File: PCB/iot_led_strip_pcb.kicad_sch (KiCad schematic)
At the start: 39 parts, among them J1 I2C Expansion, J2 Conn_01x03_Socket, J3 GT-USB-7010ASV, J4 Barrel_Jack_Switch_Pin3Ring, J5 TC2050-IDC_Cortex-M, J6 Conn_01x03_Socket_Solderwire, J8 UART, Q1 BSS138, SW1 RESET, SW2 FLASH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

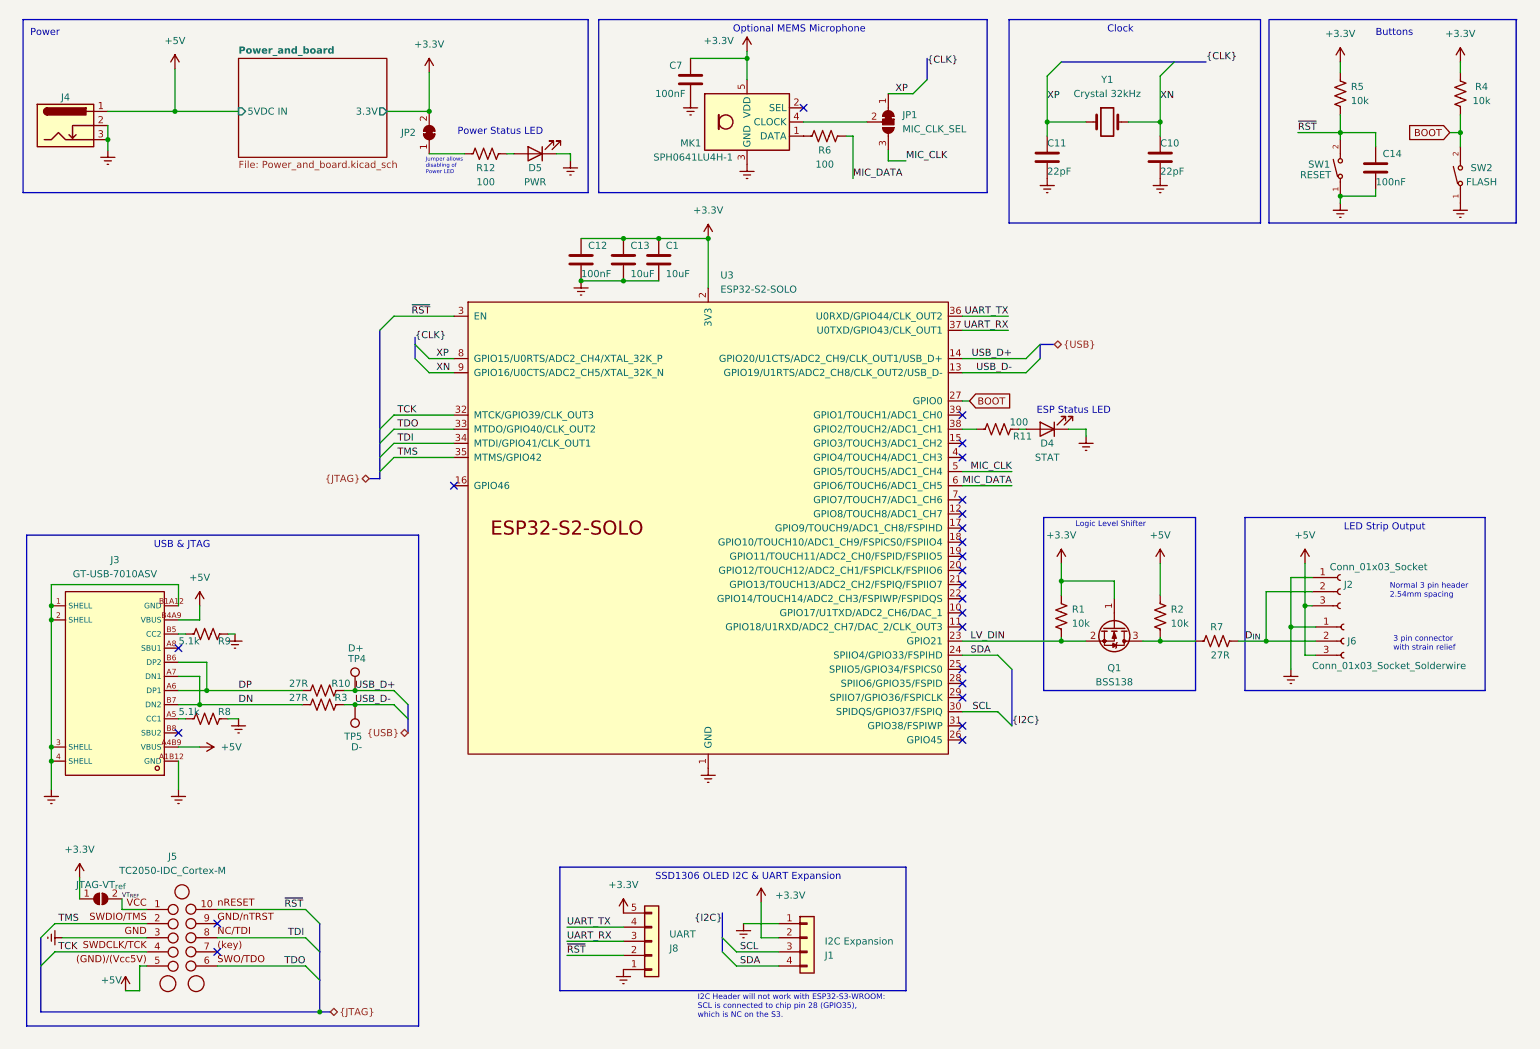
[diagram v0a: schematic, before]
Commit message: Major schematic update for v2.3
This was my first real PCB project, and looking back with a couple
months of hindsight I made some mistakes. Some best practices for
driving WS2812B strips weren't followed in my original version, and
I've updated the schematic to reflect what I've learned and what
improvements needed to be made.

* Warning added to README about current version
* Schematic reorganized into tiles
* RTC clock removed
* OLED and I2C headers removed
* JTAG footprint updated
* Pin header output replaced with screw terminal
* Hole size for power injection header increased
* Added whole system fuse and PTC fuse to protect ESP32
* Added reverse polarity protection and re-added ability to disconnect
  USB Vbus from Vdd, so it's possible to program when the strip is
  connected to 12V without frying your computer

There are a couple other improvements that could still be made to the
schematic (removing the solderwire connector for example) but it remains to
be seen if I'm going to go back and re-design the PCB to incorporate
these changes or move onto newer projects.
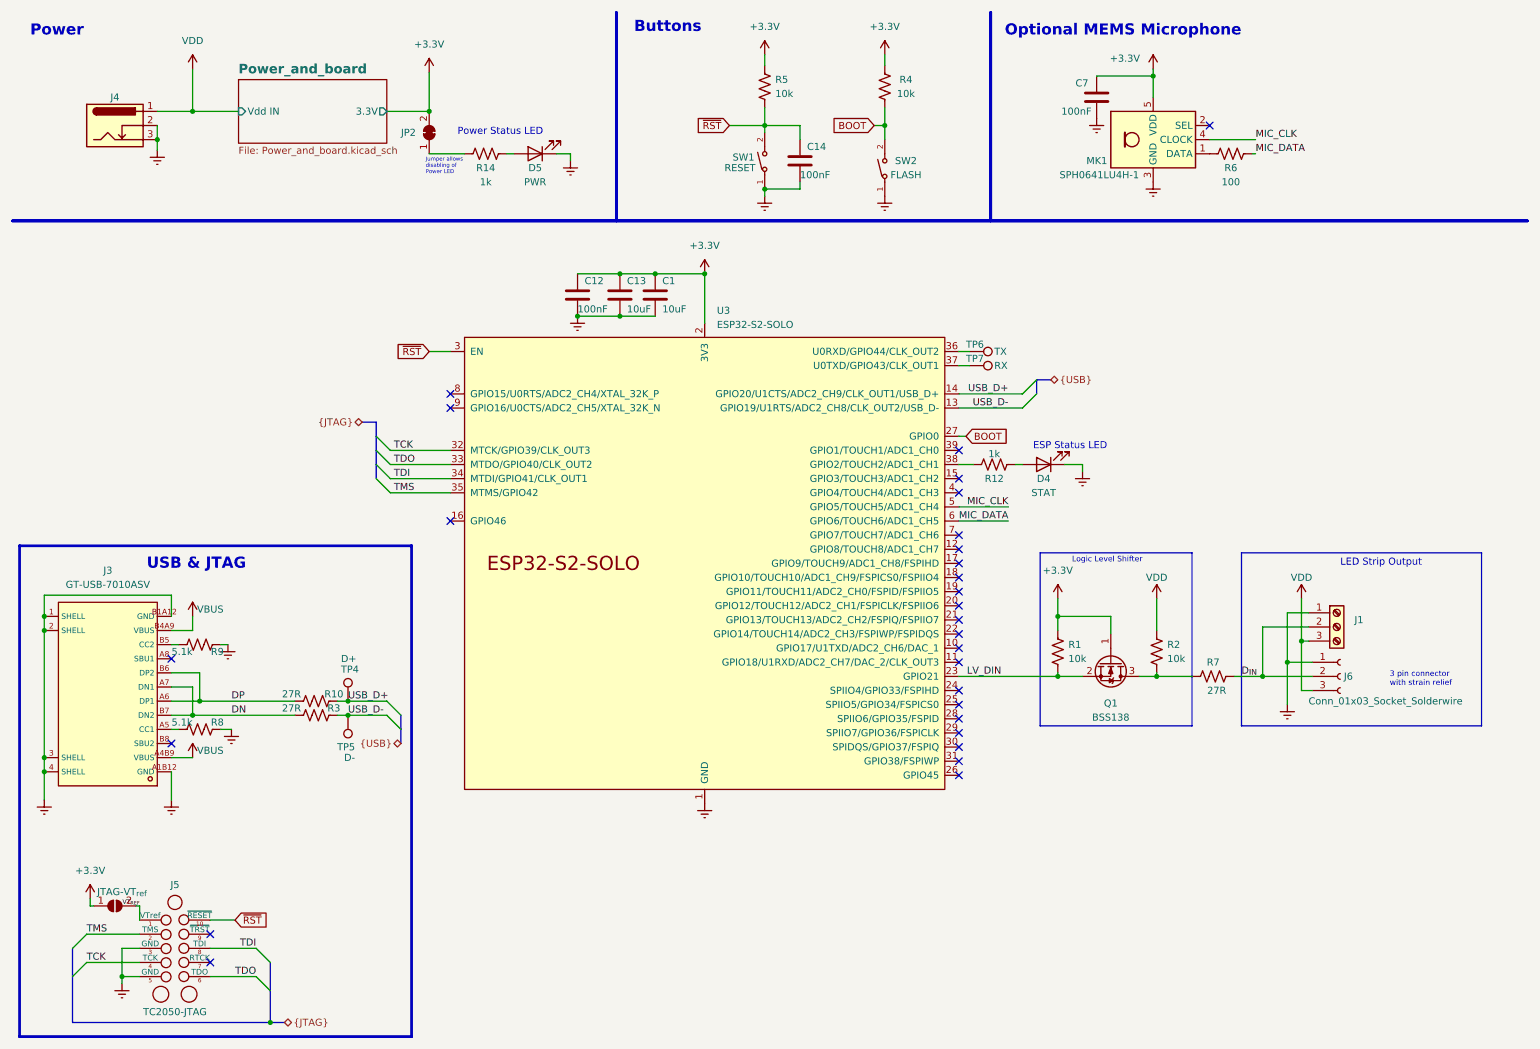
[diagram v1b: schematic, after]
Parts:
- removed C10, C11: 22pF, Capacitor_SMD:C_0805_2012Metric_Pad1.18x1.45mm_HandSolder, symbol Device:C
- removed J1: I2C Expansion, Connector_PinHeader_2.54mm:PinHeader_1x04_P2.54mm_Vertical, symbol Connector_Generic:Conn_01x04
- removed J2: Conn_01x03_Socket, Connector_PinHeader_2.54mm:PinHeader_1x03_P2.54mm_Vertical, symbol Connector:Conn_01x03_Socket
- removed J5: TC2050-IDC_Cortex-M, Connector:Tag-Connect_TC2050-IDC-FP_2x05_P1.27mm_Vertical, symbol Tag-Connect:TC2050-IDC_Cortex-M
- removed J8: UART, footprint:5 Pin Pad array, symbol Connector_Generic:Conn_01x05
- removed JP1: MIC_CLK_SEL, Jumper:SolderJumper-3_P1.3mm_Bridged12_RoundedPad1.0x1.5mm, symbol Jumper:SolderJumper_3_Bridged12
- removed R11: 100, Resistor_SMD:R_0805_2012Metric_Pad1.20x1.40mm_HandSolder, symbol Device:R_US
- removed Y1: Crystal 32kHz, Crystal:Crystal_SMD_3215-2Pin_3.2x1.5mm, symbol Device:Crystal
- added J1: Screw_Terminal_01x03, TerminalBlock:TerminalBlock_bornier-3_P5.08mm, symbol Connector:Screw_Terminal_01x03
- added J5: TC2050-JTAG, Connector:Tag-Connect_TC2050-IDC-FP_2x05_P1.27mm_Vertical, symbol jmux-kicadlib:TC2050-JTAG
- added R14: 1k, Resistor_SMD:R_0805_2012Metric_Pad1.20x1.40mm_HandSolder, symbol Device:R_US
- added TP6: TX, TestPoint:TestPoint_Pad_D1.5mm, symbol Connector:TestPoint
- added TP7: RX, TestPoint:TestPoint_Pad_D1.5mm, symbol Connector:TestPoint
- R12: value 100 -> 1k; LCSC C17408 -> C17513; Vendor https://jlcpcb.com/partdetail/18096-0805W8F1000T5E/C17408 -> (none)
- TP4, TP5: footprint TestPoint:TestPoint_Pad_D1.0mm -> TestPoint:TestPoint_Pad_D1.5mm
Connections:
- net D_{IN}: now also J1.2 (Pin_2)
- net Earth: now also J1.1 (Pin_1), J5.3 (GND), J5.5 (GND)
- net MIC_CLK: now also MK1.4 (CLOCK)
- net TCK: now also J5.4 (TCK)
- net TDI: now also J5.8 (TDI)
- net TDO: now also J5.6 (TDO)
- net TMS: now also J5.2 (TMS)
- net VT_{REF}: now also J5.1 (VTref)
- net ~{RST}: now also J5.10 (~{RESET})
- net at D4.2 (A): now also R12.1
- net at D5.2 (A): now also R14.1; no longer R12.1
- net at JP2.1 (A): now also R14.2; no longer R12.2
- net at U3.38 (GPIO2/TOUCH2/ADC1_CH1): now also R12.2
- net +5V renamed VDD
- net VDD: now also J1.3 (Pin_3); no longer J3.A4B9 (VBUS), J3.B4A9 (VBUS)
- net SCL: no longer names the net of U3.30 (SPIDQS/GPIO37/FSPIQ)
- net SDA: no longer names the net of U3.24 (SPIIO4/GPIO33/FSPIHD)
- net UART_RX: no longer names the net of U3.37 (U0TXD/GPIO43/CLK_OUT1)
- net UART_RX: now also TP7.1
- net UART_TX: no longer names the net of U3.36 (U0RXD/GPIO44/CLK_OUT2)
- net UART_TX: now also TP6.1
- net XN: no longer names the net of U3.9 (GPIO16/U0CTS/ADC2_CH5/XTAL_32K_N)
- net XP: no longer names the net of U3.8 (GPIO15/U0RTS/ADC2_CH4/XTAL_32K_P)
- new net VBUS: J3.A4B9 (VBUS), J3.B4A9 (VBUS)
- no-connect marks 24 -> 28
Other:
- sheet Power_and_board ports: added Vdd IN; removed 5VDC IN
- note removed: "Clock"
- note removed: "I2C Header will not work with ESP32-S3-WROOM: SCL is connected to chip pin 28 (GPIO35), which is NC on the S3."
- note removed: "Normal 3 pin header 2.54mm spacing"
- note removed: "SSD1306 OLED I2C & UART Expansion"
- moved on the sheet: C1, C12, C13, C14, C7, D4, J3, J4, J6, MK1, Q1, R1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

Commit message: Schematic and Board redesigned for new rev: v3.0
Schematic and board redone for next generation board - v3.0. Current rev is v3.0b.

* pin numbers added to PCB
* Silkscreen spot for writing board identifier in sharpie
* Silkscreen updated with more detailed information about board and pins to improve UX

* Logic level converters still present on data lines
* Selectable data line resistors added
* Moved to screw terminals instead of requiring soldered on connectors
* Logic level shifter IC - 74AHCT125 - Added. Two channels in use, one broken out to pads.

* System blade fuse added, along with PTC fuse for ESP itself.
* selectable board voltage - 5 or 12V
* Power inejction headers upgraded - board can be powered
    externally, or can be used as an (unfused) source of power for other LEDs!
* 5V LDO added to support logic level shifter IC

Kicad project library format changed based on since-gained kicad experience
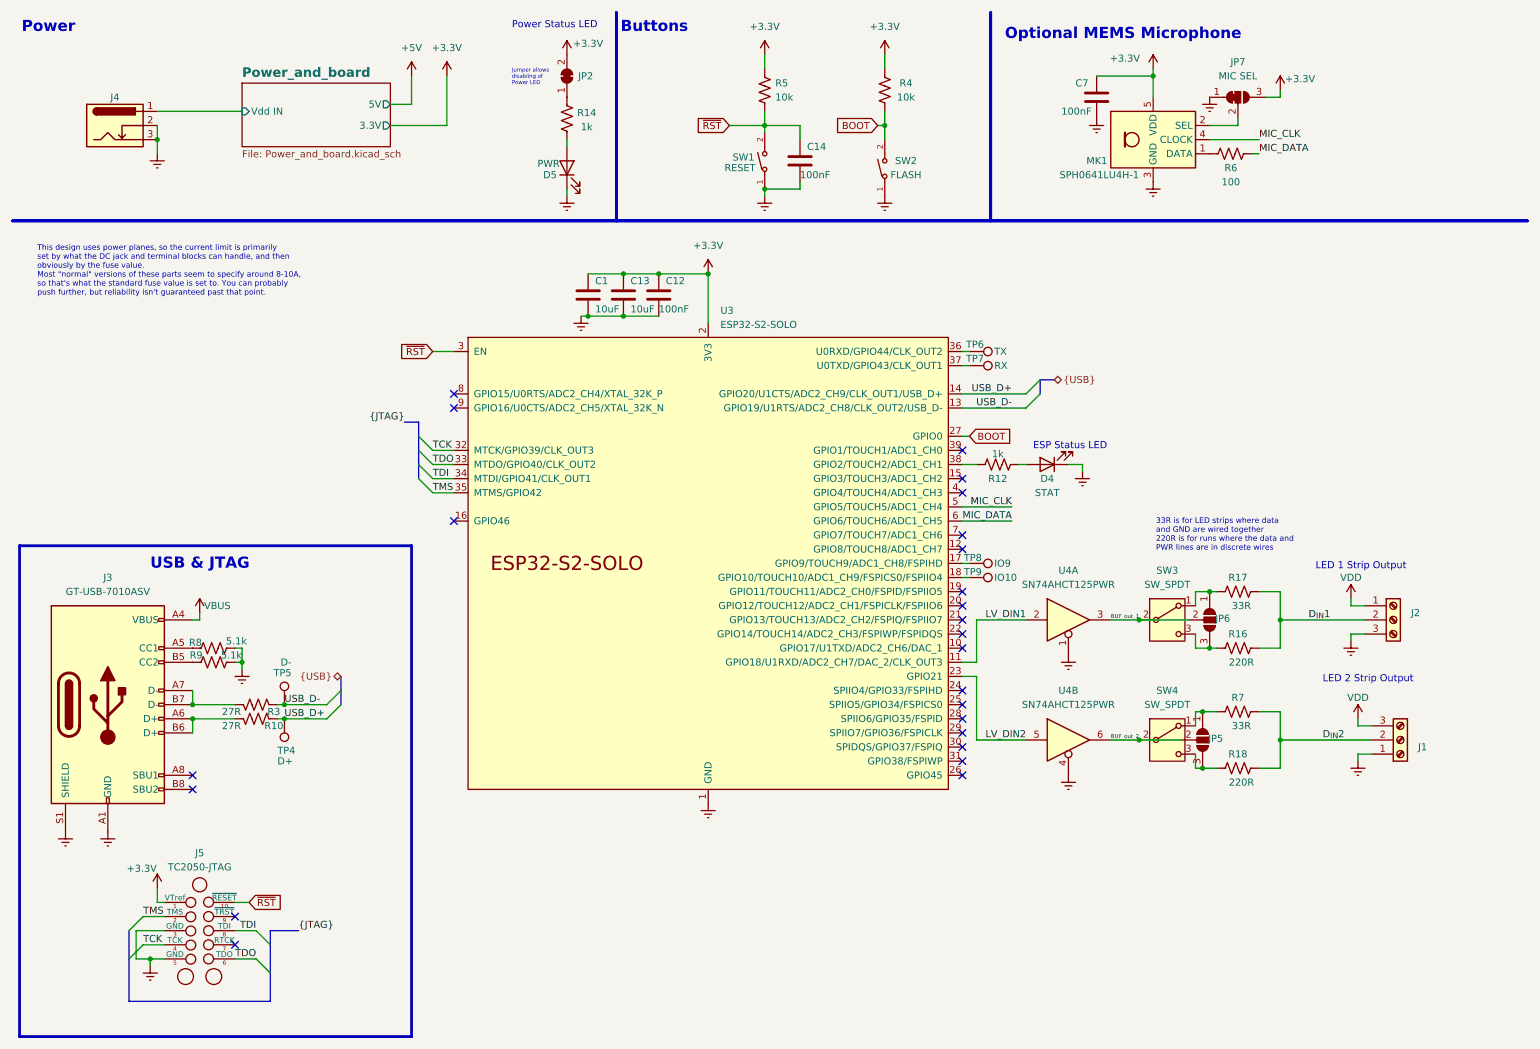
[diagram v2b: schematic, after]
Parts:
- removed J3: GT-USB-7010ASV, footprint:USB-C-SMD_G-SWITCH_GT-USB-7010ASV, symbol gt-usb_lib:GT-USB-7010ASV
- removed J6: Conn_01x03_Socket_Solderwire, Connector_Wire:SolderWire-0.5sqmm_1x03_P4.6mm_D0.9mm_OD2.1mm_Relief, symbol Connector:Conn_01x03_Socket
- removed JP7: JTAG-VT_{ref}, Jumper:SolderJumper-2_P1.3mm_Open_RoundedPad1.0x1.5mm, symbol Jumper:SolderJumper_2_Open
- removed Q1: BSS138, Package_TO_SOT_SMD:SOT-23, symbol Transistor_FET:BSS138
- removed R1, R2: 10k, Resistor_SMD:R_0805_2012Metric_Pad1.20x1.40mm_HandSolder, symbol Device:R_US
- added J2: Screw_Terminal_01x03, TerminalBlock:TerminalBlock_bornier-3_P5.08mm, symbol Connector:Screw_Terminal_01x03
- added J3: GT-USB-7010ASV, jmux-footprints:USB-C-GT7010_FIXED, symbol Connector:USB_C_Receptacle_USB2.0_16P
- added JP5, JP6: SolderJumper_3_Open, Jumper:SolderJumper-3_P1.3mm_Open_Pad1.0x1.5mm, symbol Jumper:SolderJumper_3_Open
- added JP7: MIC SEL, Jumper:SolderJumper-3_P1.3mm_Bridged12_RoundedPad1.0x1.5mm, symbol Jumper:SolderJumper_3_Bridged12
- added R16, R18: 220R, Resistor_SMD:R_0805_2012Metric_Pad1.20x1.40mm_HandSolder, symbol Device:R_US
- added R17: 33R, Resistor_SMD:R_0805_2012Metric_Pad1.20x1.40mm_HandSolder, symbol Device:R_US
- added SW3, SW4: SW_SPDT, Button_Switch_SMD:SW_SPDT_PCM12, symbol Switch:SW_SPDT
- added TP8: IO9, TestPoint:TestPoint_Pad_D1.5mm, symbol Connector:TestPoint
- added TP9: IO10, TestPoint:TestPoint_Pad_D1.5mm, symbol Connector:TestPoint
- added U4: SN74AHCT125PWR, Package_SO:TSSOP-14_4.4x5mm_P0.65mm, symbol 74xx:74AHCT125
- J5: footprint Connector:Tag-Connect_TC2050-IDC-FP_2x05_P1.27mm_Vertical -> jmux-footprints:Tag-Connect_TC2050-IDC-FP_2x05_P1.27mm_Vertical
- R7: value 27R -> 33R; LCSC C17594 -> C17634; Vendor https://www.lcsc.com/product-detail/Chip-Resistor-Surface-M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 -> https://jlcpcb.com/partdetail/18322-0805W8F330JT5E/C17634
- U3: footprint Espressif:ESP32-S2-SOLO -> PCM_Espressif:ESP32-S2-SOLO
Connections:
- net VT_{REF} is gone; now on net +3.3V: J5.1 (VTref)
- net +3.3V: now also JP7.3 (B)
- net Earth: now also R9.1, J2.3 (Pin_3), J3.A1 (GND), J3.A12 (GND), J3.B1 (GND), J3.B12 (GND), J3.S1 (SHIELD), JP7.1 (A), U4.1, U4.4; no longer R9.2
- net VBUS: now also J3.A4 (VBUS), J3.A9 (VBUS), J3.B4 (VBUS), J3.B9 (VBUS)
- net VDD: now also J2.1 (Pin_1); no longer J4.1
- net at R8.1: now also J3.A5 (CC1)
- net at R7.1: now also JP5.1 (A), SW4.1 (A)
- net at MK1.2 (SEL): now also JP7.2 (C)
- net LV_DIN1: now reaches U3.11 (GPIO18/U1RXD/ADC2_CH7/DAC_2/CLK_OUT3)
- net LV_DIN1: now also U4.2
- net at U3.17 (GPIO9/TOUCH9/ADC1_CH8/FSPIHD): now also TP8.1
- net at U3.18 (GPIO10/TOUCH10/ADC1_CH9/FSPICS0/FSPIIO4): now also TP9.1
- net DN: no longer names the net of R3.1
- net DN: now also J3.A7 (D-), J3.B7 (D-)
- net DP: no longer names the net of R10.1
- net DP: now also J3.A6 (D+), J3.B6 (D+)
- net D_{IN} renamed D_{IN}2
- net D_{IN}2: now also R18.2
- net LV_DIN renamed LV_DIN2
- net LV_DIN2: now also U4.5
- new net: JP6.1 (A), R17.1, SW3.1 (A)
- new net: J3.B5 (CC2), R9.2
- new net: JP5.3 (B), R18.1, SW4.3 (C)
- new net: JP6.3 (B), R16.1, SW3.3 (C)
- new net BUF_out_1: JP6.2 (C), SW3.2 (B), U4.3
- new net BUF_out_2: JP5.2 (C), SW4.2 (B), U4.6
- new net D_{IN}1: J2.2 (Pin_2), R16.2, R17.2
- new net Power_and_board/Vdd IN: J4.1
- no-connect marks 28 -> 24
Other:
- sheet Power_and_board ports: added 5V; removed none
- note added: "33R is for LED strips where data and GND are wired together 220R is for runs where the data and PWR lines are in discrete wires"
- note added: "LED 1 Strip Output"
- note added: "LED 2 Strip Output"
- note added: "This design uses power planes, so the current limit is primarily set by what the DC jack and terminal blocks can handle, and then obviously by the fuse value. Most "normal" versions of these parts seem to specify around 8-10A, so that's what the standard fuse value is set to. You can probably push further, but reliability isn't guaranteed past that point."
- note removed: "3 pin connector with strain relief"
- note removed: "LED Strip Output"
- note removed: "Logic Level Shifter"
- title: Spotify Neopixel Visualizer -> IoT LEDDriver HW
- moved on the sheet: C1, C12, C13, D4, D5, J1, JP2, R10, R12, R14, R3, R4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
